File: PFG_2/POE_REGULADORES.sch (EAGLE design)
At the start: 185 parts, among them J1 1-406541-1, J10 OSTVN04A150, J2 AMPS_Connect, J3 Port Current, J4 OSTVN04A150, J5 TB001-500-02BE, J6 OSTVN02A150, J7 OSTVN02A150, J8 TB001-500-02BE, J9 TB001-500-02BE, Q1 FDN8601, Q2 FDN8601, Q3 FDN8601, Q4 FDN8601, Q5 CSD18533Q5A, Q6 CSD18533Q5A, T1 750313355, U1 7490220122, U10 12V, U11 FCX493TA, U12 TL431AIDBVR, U13 LM5165DRCR, U14 ENC28J60-I/SP, U2 TPS2373-3RGWT, U3 UCC2897APW, U4 12V, U5 FCX493TA, U6 TCMT1107, U7 MMBT3906, U8 FDMS86250, U9 IRFR9220PBF, Y1 Crystal_25Mhz

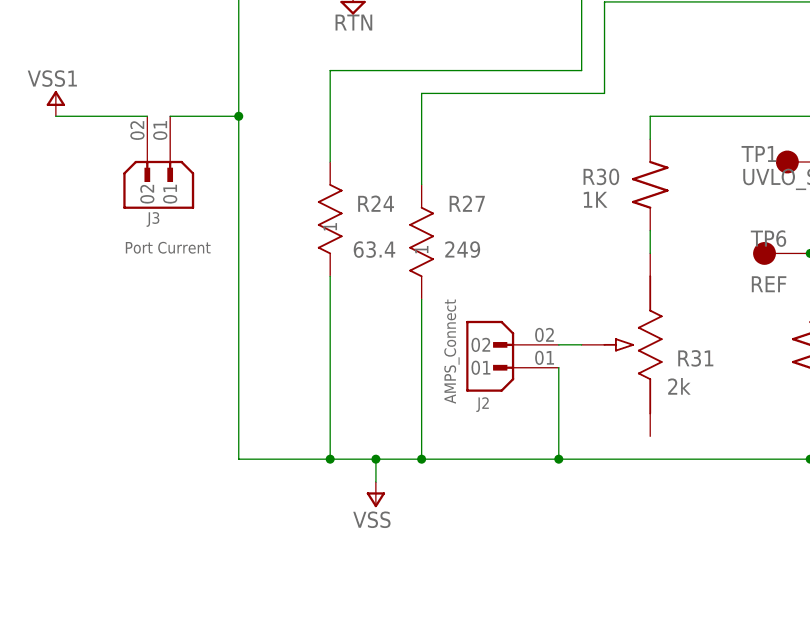
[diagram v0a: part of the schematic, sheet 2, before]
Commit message: Colocados componentes y planos RTN, GND, VDD, VSS, 3V3, 12V
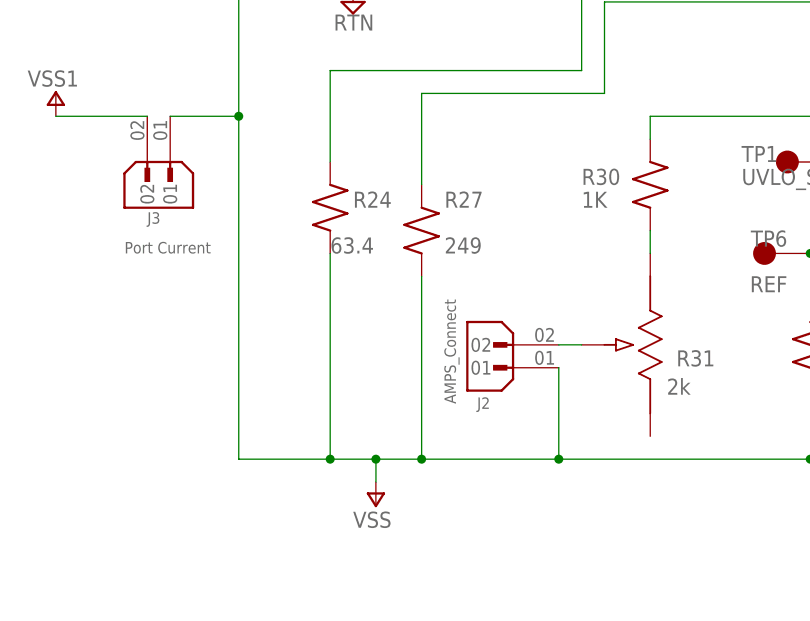
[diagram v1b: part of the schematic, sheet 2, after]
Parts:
- R24, R27: device R24:MFR-25FBF52-63R4 -> RC1206FR-071ML:RC1206FR-071ML
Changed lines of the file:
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@@
 <part name="P+24" library="supply_S" deviceset="VSS" device=""/>
 <part name="R62" library="RC1206FR-071ML" deviceset="RC1206FR-071ML" device="" value="53.6k"/>
-<part name="R24" library="R24" deviceset="MFR-25FBF52-63R4" device="" value="63.4"/>
-<part name="R27" library="R24" deviceset="MFR-25FBF52-63R4" device="" value="249"/>
 <part name="P-1" library="supply_S" deviceset="RTN" device=""/>
 <part name="J6" library="CON2_254MM" deviceset="OSTVN02A150" device=""/>
@@
 <part name="C3" library="C1206Y104K9RAC7800" deviceset="C1206Y104K9RAC7800" device="" value="0.1uF"/>
 <part name="C4" library="C1206Y104K9RAC7800" deviceset="C1206Y104K9RAC7800" device="" value="2.2uF"/>
+<part name="R24" library="RC1206FR-071ML" deviceset="RC1206FR-071ML" device="" value="63.4"/>
+<part name="R27" library="RC1206FR-071ML" deviceset="RC1206FR-071ML" device="" value="249"/>
 </parts>
 <sheets>
@@
 <attribute name="VALUE" x="243.83003125" y="101.593359375" size="1.778" layer="96"/>
 </instance>
-<instance part="R24" gate="A" x="63.5" y="81.28" smashed="yes" rot="R90">
-<attribute name="VALUE" x="65.9638" y="83.3628" size="1.778" layer="96" ratio="10" rot="SR0"/>
-<attribute name="NAME" x="66.3956" y="88.4428" size="1.778" layer="95" ratio="10" rot="SR0"/>
-</instance>
-<instance part="R27" gate="A" x="73.66" y="78.74" smashed="yes" rot="R90">
-<attribute name="VALUE" x="76.1238" y="83.3628" size="1.778" layer="96" ratio="10" rot="SR0"/>
-<attribute name="NAME" x="76.5556" y="88.4428" size="1.778" layer="95" ratio="10" rot="SR0"/>
-</instance>
 <instance part="P-1" gate="G$1" x="226.06" y="132.08" smashed="yes">
 <attribute name="VALUE" x="223.901" y="128.905" size="1.778" layer="96"/>
@@
 <instance part="J9" gate="G$1" x="238.76" y="134.62" smashed="yes">
 <attribute name="NAME" x="233.18" y="139.7" size="1.778" layer="95"/>
+</instance>
+<instance part="R24" gate="G$1" x="63.5" y="88.9" smashed="yes" rot="R90">
+<attribute name="NAME" x="66.035559375" y="88.90148125" size="1.778" layer="95"/>
+<attribute name="VALUE" x="63.49003125" y="83.813359375" size="1.778" layer="96"/>
+</instance>
+<instance part="R27" gate="G$1" x="73.66" y="86.36" smashed="yes" rot="R90">
+<attribute name="NAME" x="76.195559375" y="88.90148125" size="1.778" layer="95"/>
+<attribute name="VALUE" x="76.19003125" y="83.813359375" size="1.778" layer="96"/>
 </instance>
 </instances>
@@
 <wire x1="91.44" y1="104.14" x2="63.5" y2="104.14" width="0.1524" layer="91"/>
 <wire x1="63.5" y1="93.98" x2="63.5" y2="104.14" width="0.1524" layer="91"/>
-<pinref part="R24" gate="A" pin="2"/>
+<pinref part="R24" gate="G$1" pin="2"/>
 </segment>
 </net>
@@
 <wire x1="93.98" y1="111.76" x2="93.98" y2="101.6" width="0.1524" layer="91"/>
 <wire x1="73.66" y1="91.44" x2="73.66" y2="101.6" width="0.1524" layer="91"/>
-<pinref part="R27" gate="A" pin="2"/>
+<pinref part="R27" gate="G$1" pin="2"/>
 </segment>
 </net>
@@
 <wire x1="116.84" y1="68.58" x2="116.84" y2="60.96" width="0.1524" layer="91"/>
 <junction x="116.84" y="60.96"/>
-<pinref part="R24" gate="A" pin="1"/>
-<wire x1="63.5" y1="81.28" x2="63.5" y2="60.96" width="0.1524" layer="91"/>
+<wire x1="63.5" y1="83.82" x2="63.5" y2="60.96" width="0.1524" layer="91"/>
 <junction x="63.5" y="60.96"/>
-<pinref part="R27" gate="A" pin="1"/>
-<wire x1="73.66" y1="78.74" x2="73.66" y2="60.96" width="0.1524" layer="91"/>
+<wire x1="73.66" y1="81.28" x2="73.66" y2="60.96" width="0.1524" layer="91"/>
 <junction x="73.66" y="60.96"/>
-</segment>
-<segment>
+<pinref part="R24" gate="G$1" pin="1"/>
+<pinref part="R27" gate="G$1" pin="1"/>
+</segment>
+<segment>
